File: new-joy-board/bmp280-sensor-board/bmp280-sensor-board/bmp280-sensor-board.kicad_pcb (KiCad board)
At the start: 2 copper layers, 25.4 x 14.7 mm, 9 parts, among them J1 Conn_01x05, U1 TPS76933, U2 bmp280-board, U3 P82B715

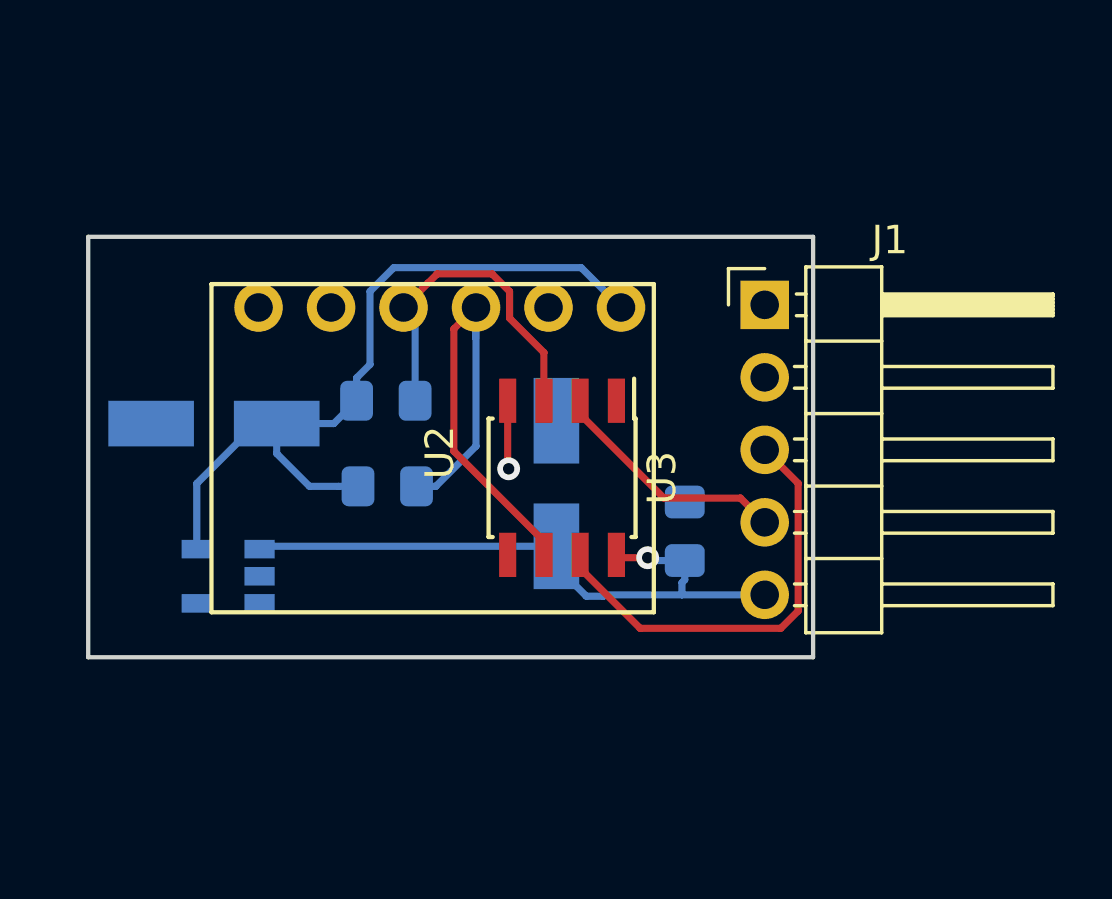
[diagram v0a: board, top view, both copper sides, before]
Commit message: Added mounting-holes
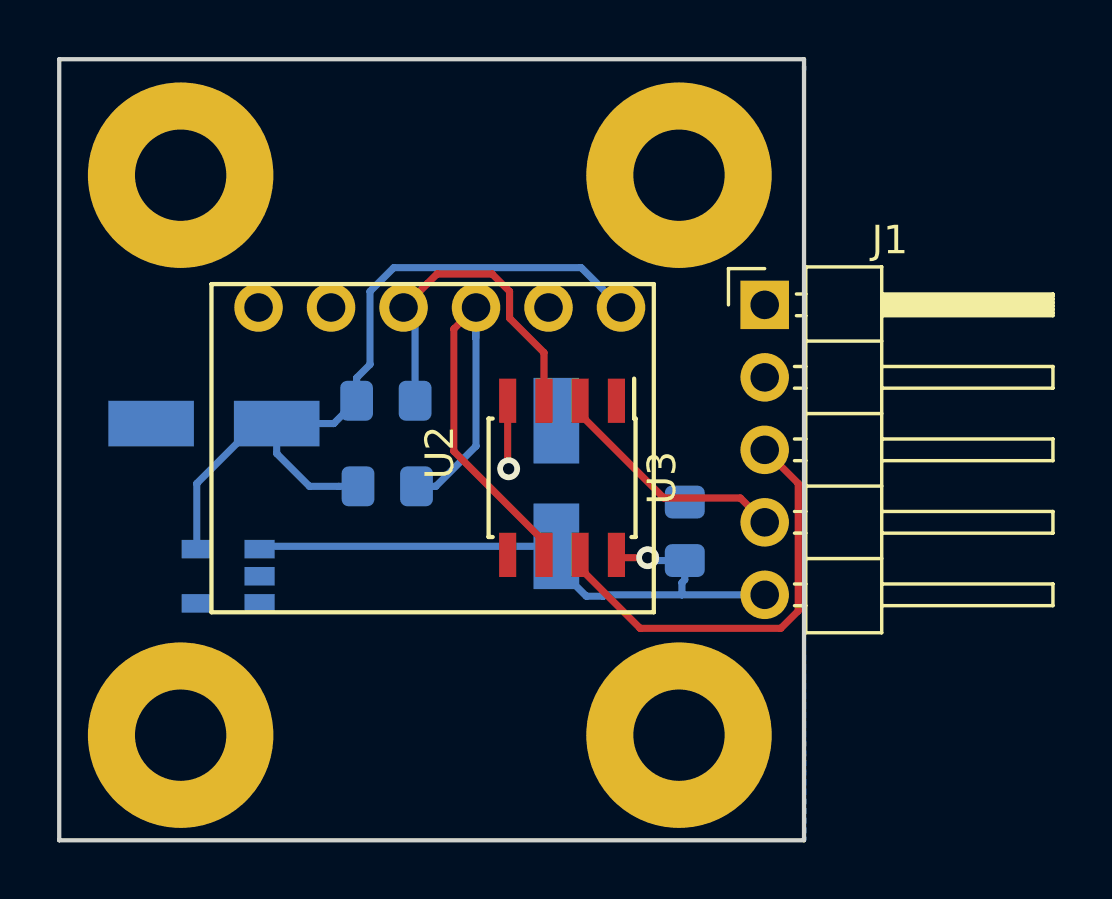
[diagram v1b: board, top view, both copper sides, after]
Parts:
- added REF**: VAL**, new-joy:z_MountPTH_3mm, F.Cu at (98.2, 59.1)
- added REF**: VAL**, new-joy:z_MountPTH_3mm, F.Cu at (115.7, 59.1)
- added REF**: VAL**, new-joy:z_MountPTH_3mm, F.Cu at (115.7, 39.5)
- added REF**: VAL**, new-joy:z_MountPTH_3mm, F.Cu at (98.2, 39.5)
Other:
- board size 25.4 x 14.7 mm -> 26.1 x 27.4 mm
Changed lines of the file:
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@@
   (general
     (thickness 1.6)
-    (drawings 4)
+    (drawings 5)
     (tracks 62)
     (zones 0)
-    (modules 9)
+    (modules 13)
     (nets 14)
   )
@@
     (add_net "Net-(U3-Pad1)")
     (add_net "Net-(U3-Pad5)")
+  )
+  (module new-joy:z_MountPTH_3mm (layer F.Cu)
+    (at 98.2345 59.1185)
+    (fp_text reference REF** (at 0 0.125) (layer F.Fab)
+      (effects (font (size 0.1 0.1) (thickness 0.01)))
+    )
+    (fp_text value VAL** (at 0 -0.125) (layer F.Fab)
+      (effects (font (size 0.1 0.1) (thickness 0.01)))
+    )
+    (fp_line (start -3.1 0) (end 3.1 0) (layer Cmts.User) (width 0.05))
+    (fp_line (start 0 -3.1) (end 0 3.1) (layer Cmts.User) (width 0.05))
+    (fp_circle (center 0 0) (end 3.5 0) (layer F.CrtYd) (width 0.05))
+    (fp_text user %R (at 0 0 180) (layer Eco1.User)
+      (effects (font (size 0.3 0.3) (thickness 0.03)))
+    )
+    (pad 1 thru_hole circle (at 0 0) (size 6.5 6.5) (drill 3.2) (layers *.Cu *.Mask))
+  )
+  (module new-joy:z_MountPTH_3mm (layer F.Cu)
+    (at 115.697 59.1185)
+    (fp_text reference REF** (at 0 0.125) (layer F.Fab)
+      (effects (font (size 0.1 0.1) (thickness 0.01)))
+    )
+    (fp_text value VAL** (at 0 -0.125) (layer F.Fab)
+      (effects (font (size 0.1 0.1) (thickness 0.01)))
+    )
+    (fp_text user %R (at 0 0 180) (layer Eco1.User)
+      (effects (font (size 0.3 0.3) (thickness 0.03)))
+    )
+    (fp_circle (center 0 0) (end 3.5 0) (layer F.CrtYd) (width 0.05))
+    (fp_line (start 0 -3.1) (end 0 3.1) (layer Cmts.User) (width 0.05))
+    (fp_line (start -3.1 0) (end 3.1 0) (layer Cmts.User) (width 0.05))
+    (pad 1 thru_hole circle (at 0 0) (size 6.5 6.5) (drill 3.2) (layers *.Cu *.Mask))
+  )
+  (module new-joy:z_MountPTH_3mm (layer F.Cu)
+    (at 115.697 39.497)
+    (fp_text reference REF** (at 0 0.125) (layer F.Fab)
+      (effects (font (size 0.1 0.1) (thickness 0.01)))
+    )
+    (fp_text value VAL** (at 0 -0.125) (layer F.Fab)
+      (effects (font (size 0.1 0.1) (thickness 0.01)))
+    )
+    (fp_line (start -3.1 0) (end 3.1 0) (layer Cmts.User) (width 0.05))
+    (fp_line (start 0 -3.1) (end 0 3.1) (layer Cmts.User) (width 0.05))
+    (fp_circle (center 0 0) (end 3.5 0) (layer F.CrtYd) (width 0.05))
+    (fp_text user %R (at 0 0 180) (layer Eco1.User)
+      (effects (font (size 0.3 0.3) (thickness 0.03)))
+    )
+    (pad 1 thru_hole circle (at 0 0) (size 6.5 6.5) (drill 3.2) (layers *.Cu *.Mask))
   )
   (module Capacitor_SMD:CP_Elec_5x5.8 (layer B.Cu)
@@
       (net 8 "Net-(U2-Pad6)"))
   )
-  (gr_line (start 120.396 41.656) (end 120.396 56.388) (layer Edge.Cuts) (width 0.15))
-  (gr_line (start 94.996 41.656) (end 120.396 41.656) (layer Edge.Cuts) (width 0.15))
-  (gr_line (start 94.996 56.388) (end 94.996 41.656) (layer Edge.Cuts) (width 0.15))
-  (gr_line (start 120.396 56.388) (end 94.996 56.388) (layer Edge.Cuts) (width 0.15))
+  (module new-joy:z_MountPTH_3mm (layer F.Cu)
+    (at 98.2345 39.497)
+    (fp_text reference REF** (at 0 0.125) (layer F.Fab)
+      (effects (font (size 0.1 0.1) (thickness 0.01)))
+    )
+    (fp_text value VAL** (at 0 -0.125) (layer F.Fab)
+      (effects (font (size 0.1 0.1) (thickness 0.01)))
+    )
+    (fp_text user %R (at 0 0 180) (layer Eco1.User)
+      (effects (font (size 0.3 0.3) (thickness 0.03)))
+    )
+    (fp_circle (center 0 0) (end 3.5 0) (layer F.CrtYd) (width 0.05))
+    (fp_line (start 0 -3.1) (end 0 3.1) (layer Cmts.User) (width 0.05))
+    (fp_line (start -3.1 0) (end 3.1 0) (layer Cmts.User) (width 0.05))
+    (pad 1 thru_hole circle (at 0 0) (size 6.5 6.5) (drill 3.2) (layers *.Cu *.Mask))
+  )
+  (gr_line (start 120.0785 35.433) (end 120.0785 35.814) (layer Edge.Cuts) (width 0.15))
+  (gr_line (start 93.98 35.433) (end 120.0785 35.433) (layer Edge.Cuts) (width 0.15))
+  (gr_line (start 93.98 62.8015) (end 93.98 35.433) (layer Edge.Cuts) (width 0.15))
+  (gr_line (start 120.0785 62.8015) (end 93.98 62.8015) (layer Edge.Cuts) (width 0.15))
+  (gr_line (start 120.0785 35.687) (end 120.0785 62.8015) (layer Edge.Cuts) (width 0.15))
   (segment (start 111.4 53.2) (end 111.4 52.5) (width 0.25) (layer B.Cu) (net 1))
   (segment (start 112.45 54.25) (end 111.4 53.2) (width 0.25) (layer B.Cu) (net 1))
@@
   (zone (net 2) (net_name GND) (layer B.Cu) (hatch edge 0.508)
     (connect_pads (clearance 0.4))
-    (min_thickness 0.2)
+    (min_thickness 0.254)
     (fill yes (arc_segments 16) (thermal_gap 0.508) (thermal_bridge_width 0.508))
     (polygon
       (pts
-        (xy 94.996 41.656) (xy 120.396 41.656) (xy 120.396 56.388) (xy 94.996 56.388)
+        (xy 93.98 35.433) (xy 120.0785 35.433) (xy 120.142 62.8015) (xy 93.98 62.8015)
       )
     )
